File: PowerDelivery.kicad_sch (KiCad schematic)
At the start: 28 parts, among them J3 Screw_Terminal_01x02, Q11 PJM2309PSA, U5 TPS5401, U6 LM1117-3.3

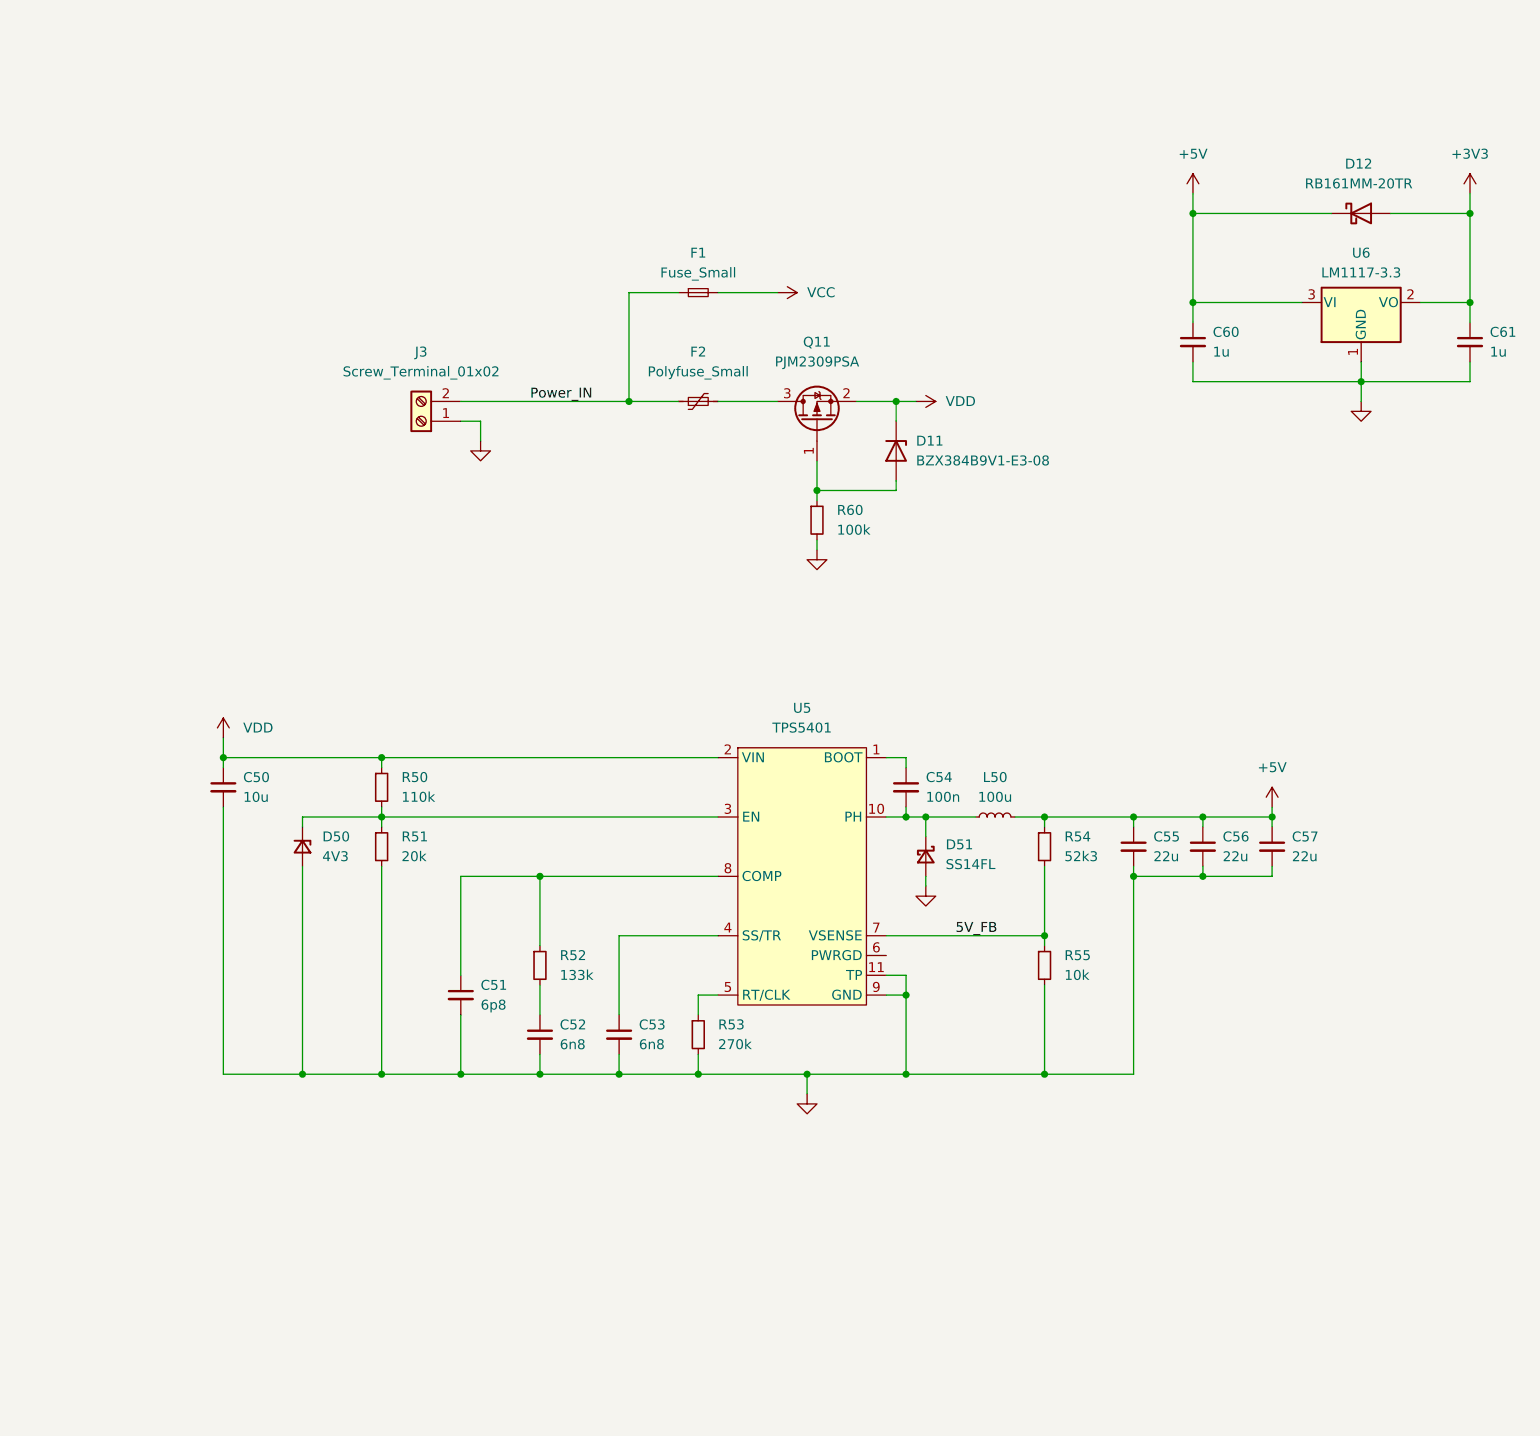
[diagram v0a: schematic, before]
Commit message: Cleaned up messy reference numbering Added labels to schematic
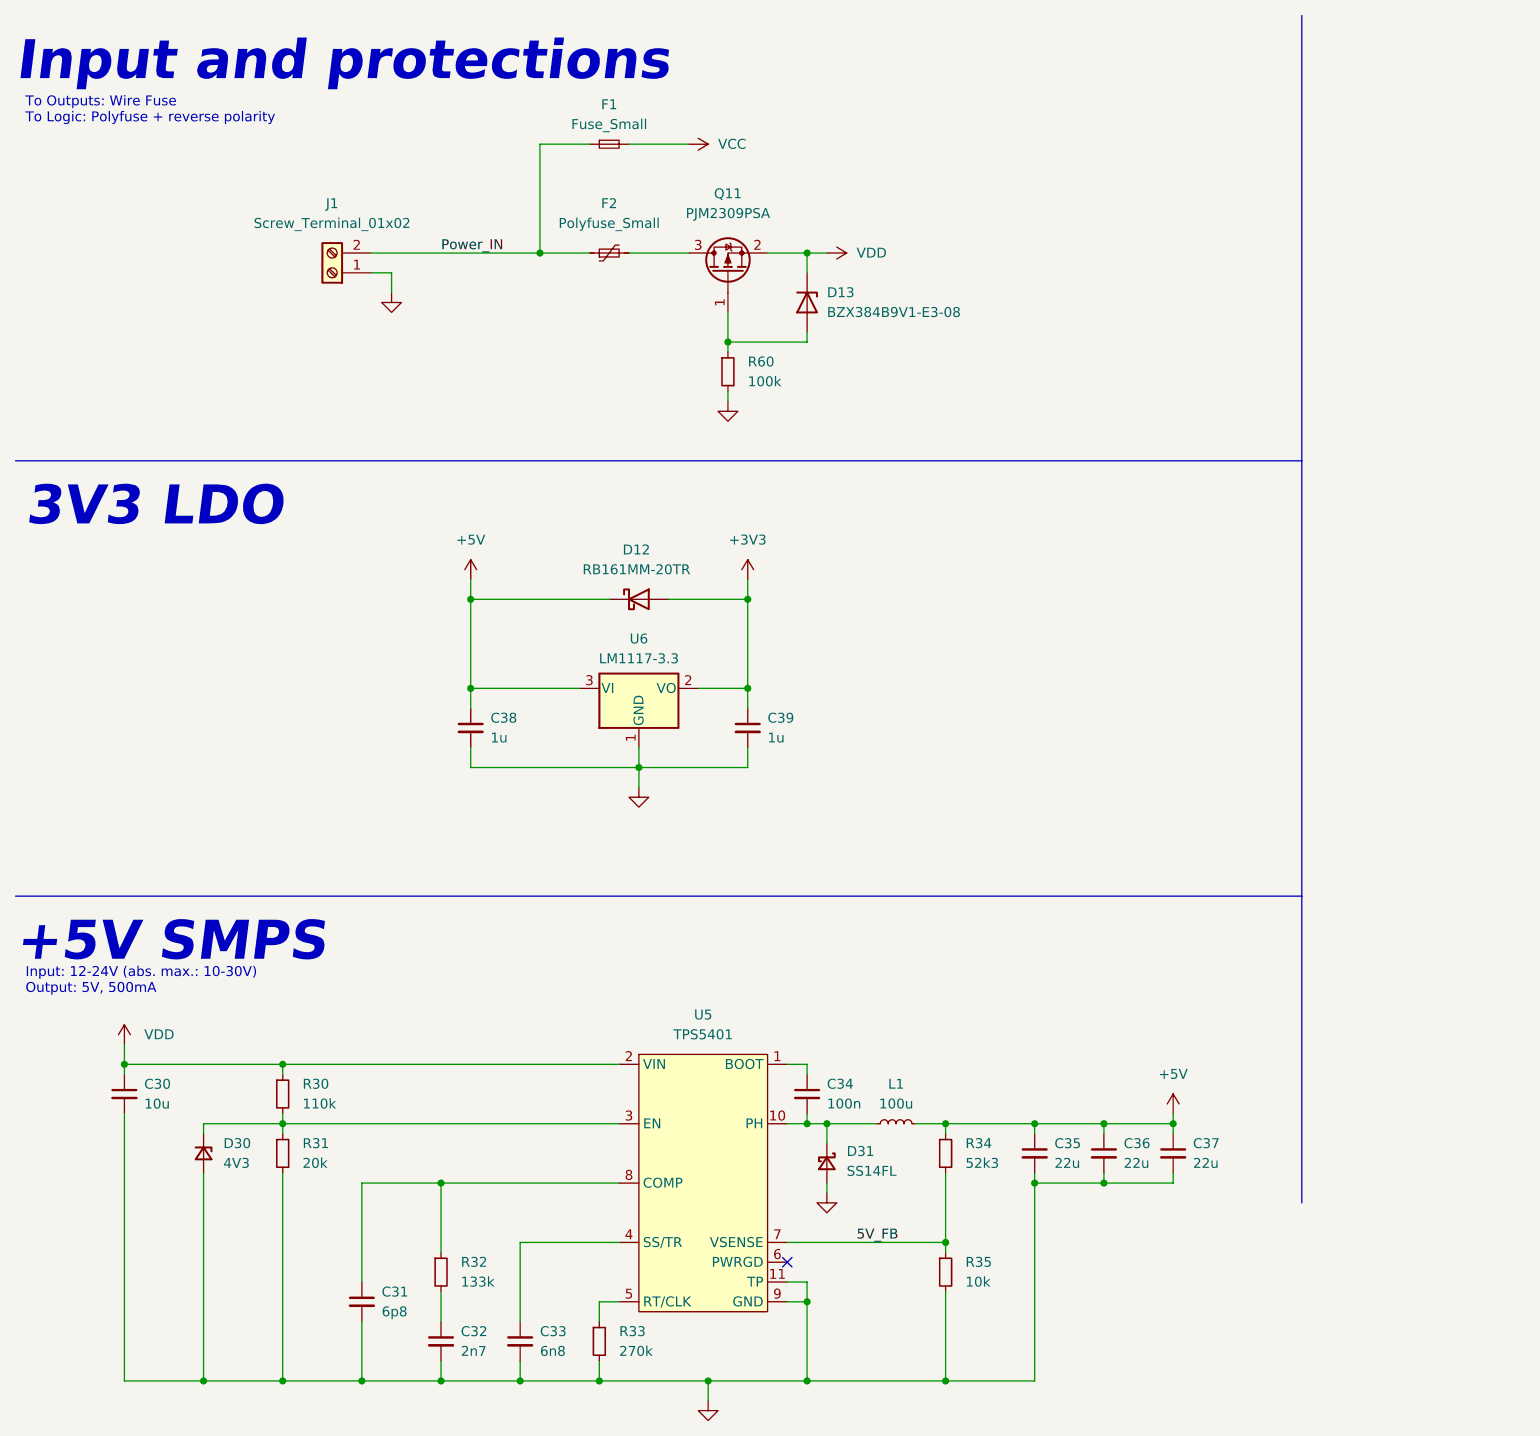
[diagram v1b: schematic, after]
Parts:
- C32: renamed from C52; value 6n8 -> 2n7
- renumbered C50 to C30, C51 to C31, C53 to C33, C54 to C34, C55 to C35, C56 to C36, C57 to C37, C60 to C38, C61 to C39, D11 to D13, D50 to D30, D51 to D31, J3 to J1, L50 to L1, R50 to R30, R51 to R31, R52 to R32, R53 to R33, R54 to R34, R55 to R35
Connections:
- no-connect marks 0 -> 1
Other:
- note added: "+5V SMPS"
- note added: "3V3 LDO"
- note added: "Input and protections"
- note added: "Input: 12-24V (abs. max.: 10-30V) Output: 5V, 500mA"
- note added: "To Outputs: Wire Fuse To Logic: Polyfuse + reverse polarity"
- moved on the sheet: C30, C31, C32, C33, C34, C35, C36, C37, C38, C39, D12, D13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

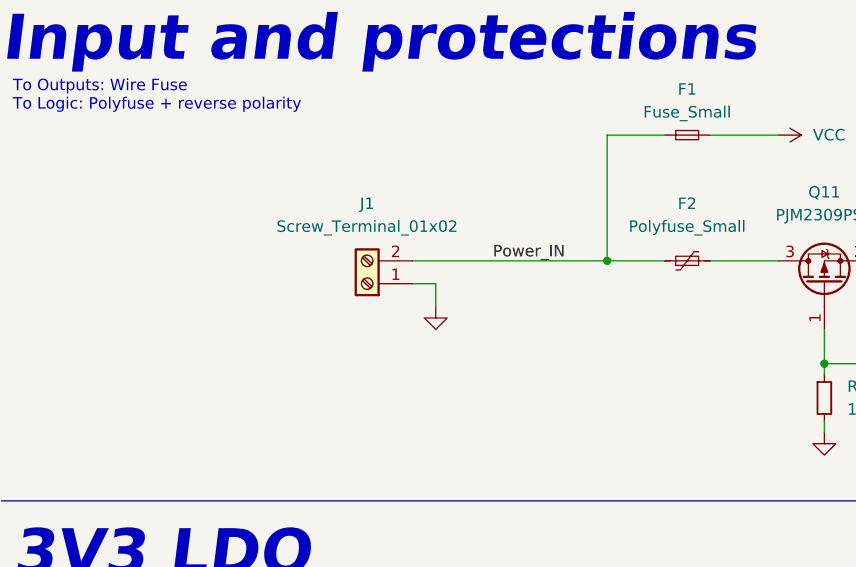
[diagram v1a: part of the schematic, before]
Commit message: Added TVS diode on power input
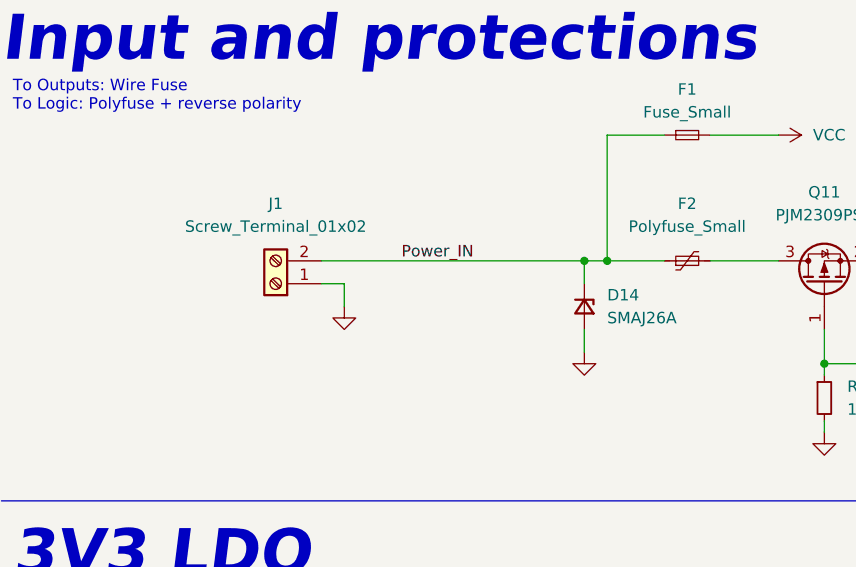
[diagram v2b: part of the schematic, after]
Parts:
- added D14: SMAJ26A, Diode_SMD:D_SMA, symbol Device:D_Zener_Small
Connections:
- net GND: now also D14.2 (A)
- net Power_IN: now also D14.1 (K)
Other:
- moved on the sheet: J1
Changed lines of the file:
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@@
   (junction (at 46.99 187.96) (diameter 0) (color 0 0 0 0)
+  )
+  (junction (at 77.47 43.18) (diameter 0) (color 0 0 0 0)
   )
   (junction (at 143.51 162.56) (diameter 0) (color 0 0 0 0)
@@
     (stroke (width 0) (type default) (color 0 0 0 0))
   )
-  (wire (pts (xy 60.96 45.72) (xy 60.96 48.26))
+  (wire (pts (xy 50.8 45.72) (xy 50.8 48.26))
     (stroke (width 0) (type default) (color 0 0 0 0))
   )
@@
     (stroke (width 0) (type default) (color 0 0 0 0))
   )
+  (wire (pts (xy 77.47 43.18) (xy 80.01 43.18))
+    (stroke (width 0) (type default) (color 0 0 0 0))
+  )
   (wire (pts (xy 106.68 101.6) (xy 106.68 99.06))
     (stroke (width 0) (type default) (color 0 0 0 0))
@@
     (stroke (width 0) (type default) (color 0 0 0 0))
   )
-  (wire (pts (xy 58.42 43.18) (xy 80.01 43.18))
-    (stroke (width 0) (type default) (color 0 0 0 0))
-  )
   (wire (pts (xy 111.76 170.18) (xy 132.08 170.18))
     (stroke (width 0) (type default) (color 0 0 0 0))
@@
     (stroke (width 0) (type default) (color 0 0 0 0))
   )
-  (wire (pts (xy 58.42 45.72) (xy 60.96 45.72))
+  (wire (pts (xy 48.26 45.72) (xy 50.8 45.72))
     (stroke (width 0) (type default) (color 0 0 0 0))
   )
@@
     (stroke (width 0) (type default) (color 0 0 0 0))
   )
+  (wire (pts (xy 77.47 43.18) (xy 77.47 45.72))
+    (stroke (width 0) (type default) (color 0 0 0 0))
+  )
   (wire (pts (xy 143.51 187.96) (xy 132.08 187.96))
     (stroke (width 0) (type default) (color 0 0 0 0))
@@
     (stroke (width 0) (type default) (color 0 0 0 0))
   )
+  (wire (pts (xy 77.47 53.34) (xy 77.47 50.8))
+    (stroke (width 0) (type default) (color 0 0 0 0))
+  )
   (polyline (pts (xy 177.8 125.73) (xy 177.8 165.1))
     (stroke (width 0) (type default) (color 0 0 0 0))
@@
   )
   (wire (pts (xy 132.08 170.18) (xy 132.08 171.45))
+    (stroke (width 0) (type default) (color 0 0 0 0))
+  )
+  (wire (pts (xy 48.26 43.18) (xy 77.47 43.18))
     (stroke (width 0) (type default) (color 0 0 0 0))
   )
@@
     (effects (font (size 1.27 1.27)) (justify left bottom))
   )
-  (label "Power_IN" (at 67.31 43.18 0)
+  (label "Power_IN" (at 57.15 43.18 0)
     (effects (font (size 1.27 1.27)) (justify left bottom))
   )
@@
     (pin "1")
   )
-  (symbol (lib_id "power:GND") (at 60.96 48.26 0) (unit 1)
-    (in_bom yes) (on_board yes) (fields_autoplaced)
-    (property "Reference" "#PWR0168" (id 0) (at 60.96 54.61 0)
-      (effects (font (size 1.27 1.27)) hide)
-    )
-    (property "Value" "GND" (id 1) (at 60.96 53.34 0)
-      (effects (font (size 1.27 1.27)) hide)
-    )
-    (property "Footprint" "" (id 2) (at 60.96 48.26 0)
-      (effects (font (size 1.27 1.27)) hide)
-    )
-    (property "Datasheet" "" (id 3) (at 60.96 48.26 0)
+  (symbol (lib_id "Device:D_Zener_Small") (at 77.47 48.26 270) (unit 1)
+    (in_bom yes) (on_board yes) (fields_autoplaced)
+    (property "Reference" "D14" (id 0) (at 80.01 46.9899 90)
+      (effects (font (size 1.27 1.27)) (justify left))
+    )
+    (property "Value" "SMAJ26A" (id 1) (at 80.01 49.5299 90)
+      (effects (font (size 1.27 1.27)) (justify left))
+    )
+    (property "Footprint" "Diode_SMD:D_SMA" (id 2) (at 77.47 48.26 90)
+      (effects (font (size 1.27 1.27)) hide)
+    )
+    (property "Datasheet" "~" (id 3) (at 77.47 48.26 90)
+      (effects (font (size 1.27 1.27)) hide)
+    )
+    (pin "1")
+    (pin "2")
+  )
+  (symbol (lib_id "power:GND") (at 50.8 48.26 0) (unit 1)
+    (in_bom yes) (on_board yes) (fields_autoplaced)
+    (property "Reference" "#PWR0168" (id 0) (at 50.8 54.61 0)
+      (effects (font (size 1.27 1.27)) hide)
+    )
+    (property "Value" "GND" (id 1) (at 50.8 53.34 0)
+      (effects (font (size 1.27 1.27)) hide)
+    )
+    (property "Footprint" "" (id 2) (at 50.8 48.26 0)
+      (effects (font (size 1.27 1.27)) hide)
+    )
+    (property "Datasheet" "" (id 3) (at 50.8 48.26 0)
+      (effects (font (size 1.27 1.27)) hide)
+    )
+    (pin "1")
+  )
+  (symbol (lib_id "power:GND") (at 77.47 53.34 0) (unit 1)
+    (in_bom yes) (on_board yes) (fields_autoplaced)
+    (property "Reference" "#PWR?" (id 0) (at 77.47 59.69 0)
+      (effects (font (size 1.27 1.27)) hide)
+    )
+    (property "Value" "GND" (id 1) (at 77.47 58.42 0)
+      (effects (font (size 1.27 1.27)) hide)
+    )
+    (property "Footprint" "" (id 2) (at 77.47 53.34 0)
+      (effects (font (size 1.27 1.27)) hide)
+    )
+    (property "Datasheet" "" (id 3) (at 77.47 53.34 0)
       (effects (font (size 1.27 1.27)) hide)
     )
@@
     (pin "1")
   )
-  (symbol (lib_id "Connector:Screw_Terminal_01x02") (at 53.34 45.72 180) (unit 1)
-    (in_bom yes) (on_board yes) (fields_autoplaced)
-    (property "Reference" "J1" (id 0) (at 53.34 36.83 0))
-    (property "Value" "Screw_Terminal_01x02" (id 1) (at 53.34 39.37 0))
-    (property "Footprint" "Connector_Phoenix_MC_HighVoltage:PhoenixContact_MC_1,5_2-GF-5.08_1x02_P5.08mm_Horizontal_ThreadedFlange" (id 2) (at 53.34 45.72 0)
-      (effects (font (size 1.27 1.27)) hide)
-    )
-    (property "Datasheet" "~" (id 3) (at 53.34 45.72 0)
-      (effects (font (size 1.27 1.27)) hide)
-    )
+  (symbol (lib_id "Connector:Screw_Terminal_01x02") (at 43.18 45.72 180) (unit 1)
+    (in_bom yes) (on_board yes) (fields_autoplaced)
+    (property "Reference" "J1" (id 0) (at 43.18 36.83 0))
+    (property "Value" "Screw_Terminal_01x02" (id 1) (at 43.18 39.37 0))
+    (property "Footprint" "Connector_Phoenix_MC_HighVoltage:PhoenixContact_MC_1,5_2-GF-5.08_1x02_P5.08mm_Horizontal_ThreadedFlange" (id 2) (at 43.18 45.72 0)
+      (effects (font (size 1.27 1.27)) hide)
+    )
+    (property "Datasheet" "~" (id 3) (at 43.18 45.72 0)
+      (effects (font (size 1.27 1.27)) hide)
+    )
